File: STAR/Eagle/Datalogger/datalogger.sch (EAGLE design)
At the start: 7 parts, among them J1 J30J-25

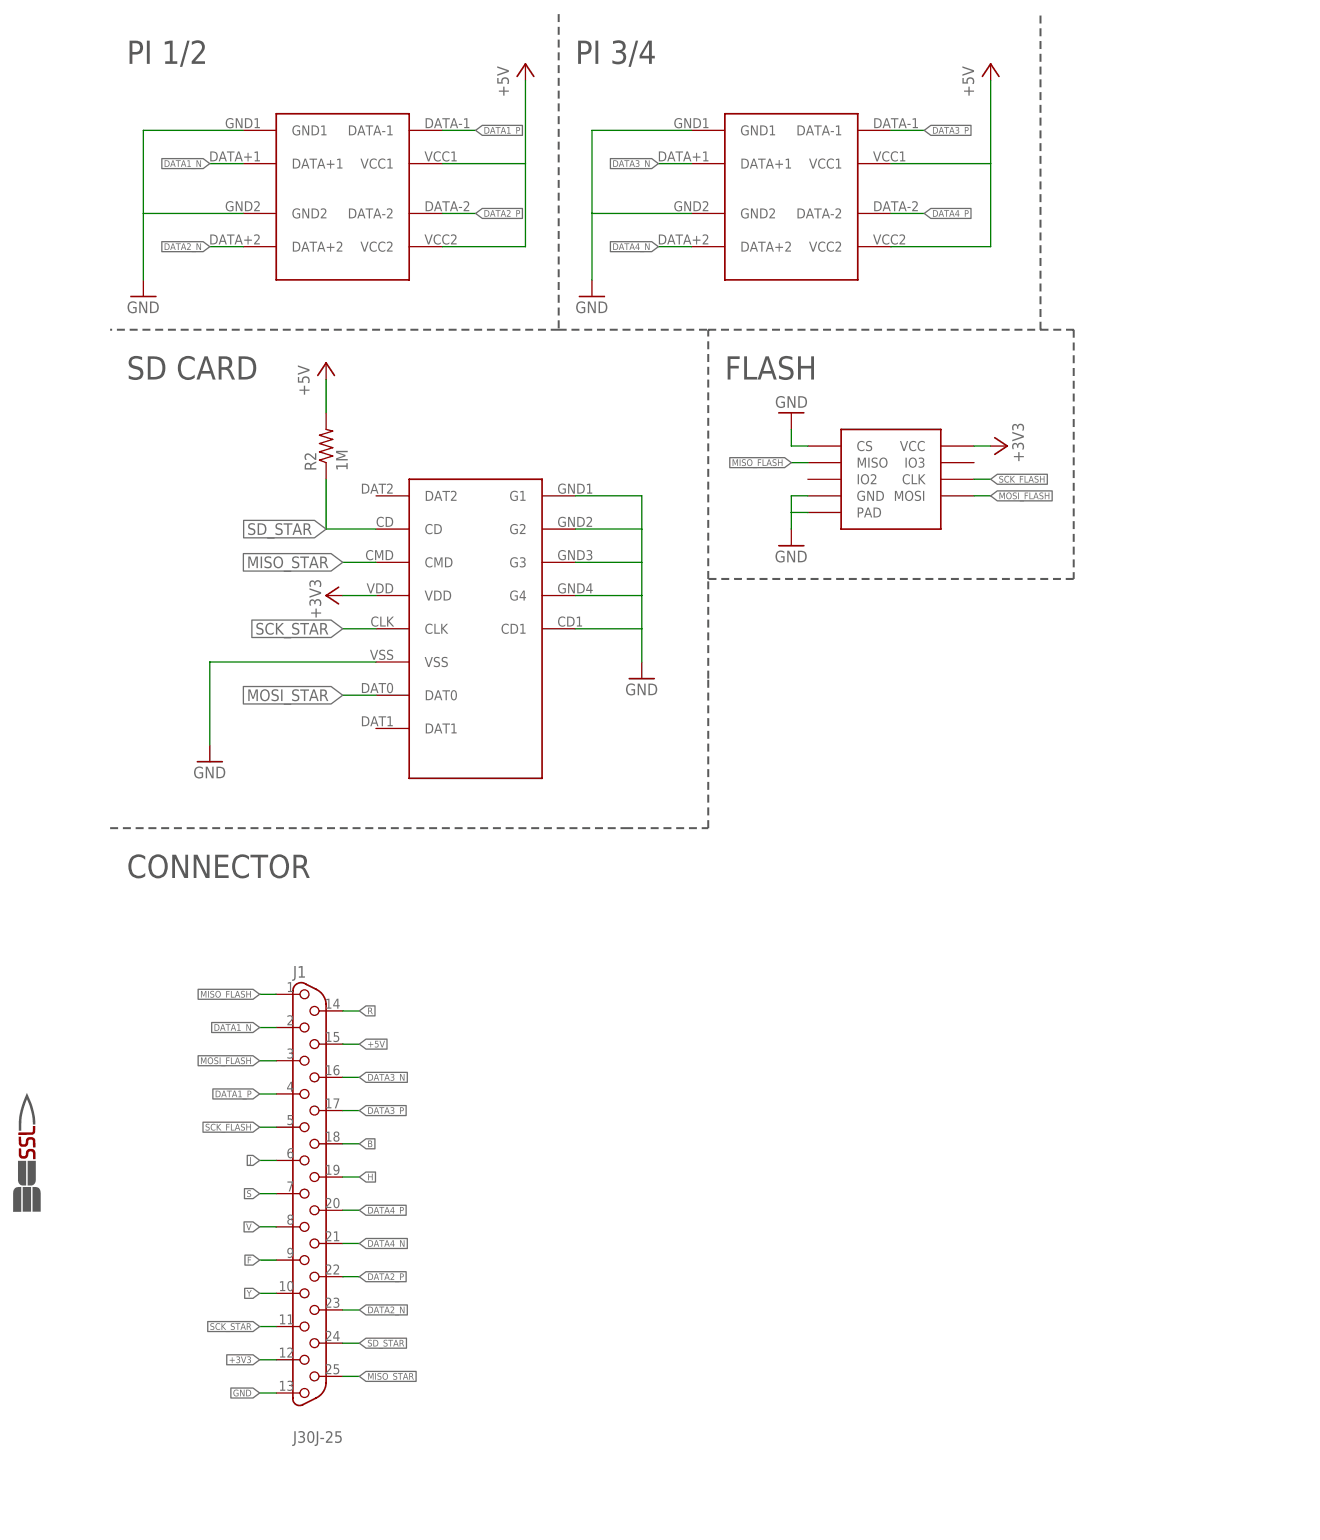
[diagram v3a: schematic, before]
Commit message: datalogger differential pairs
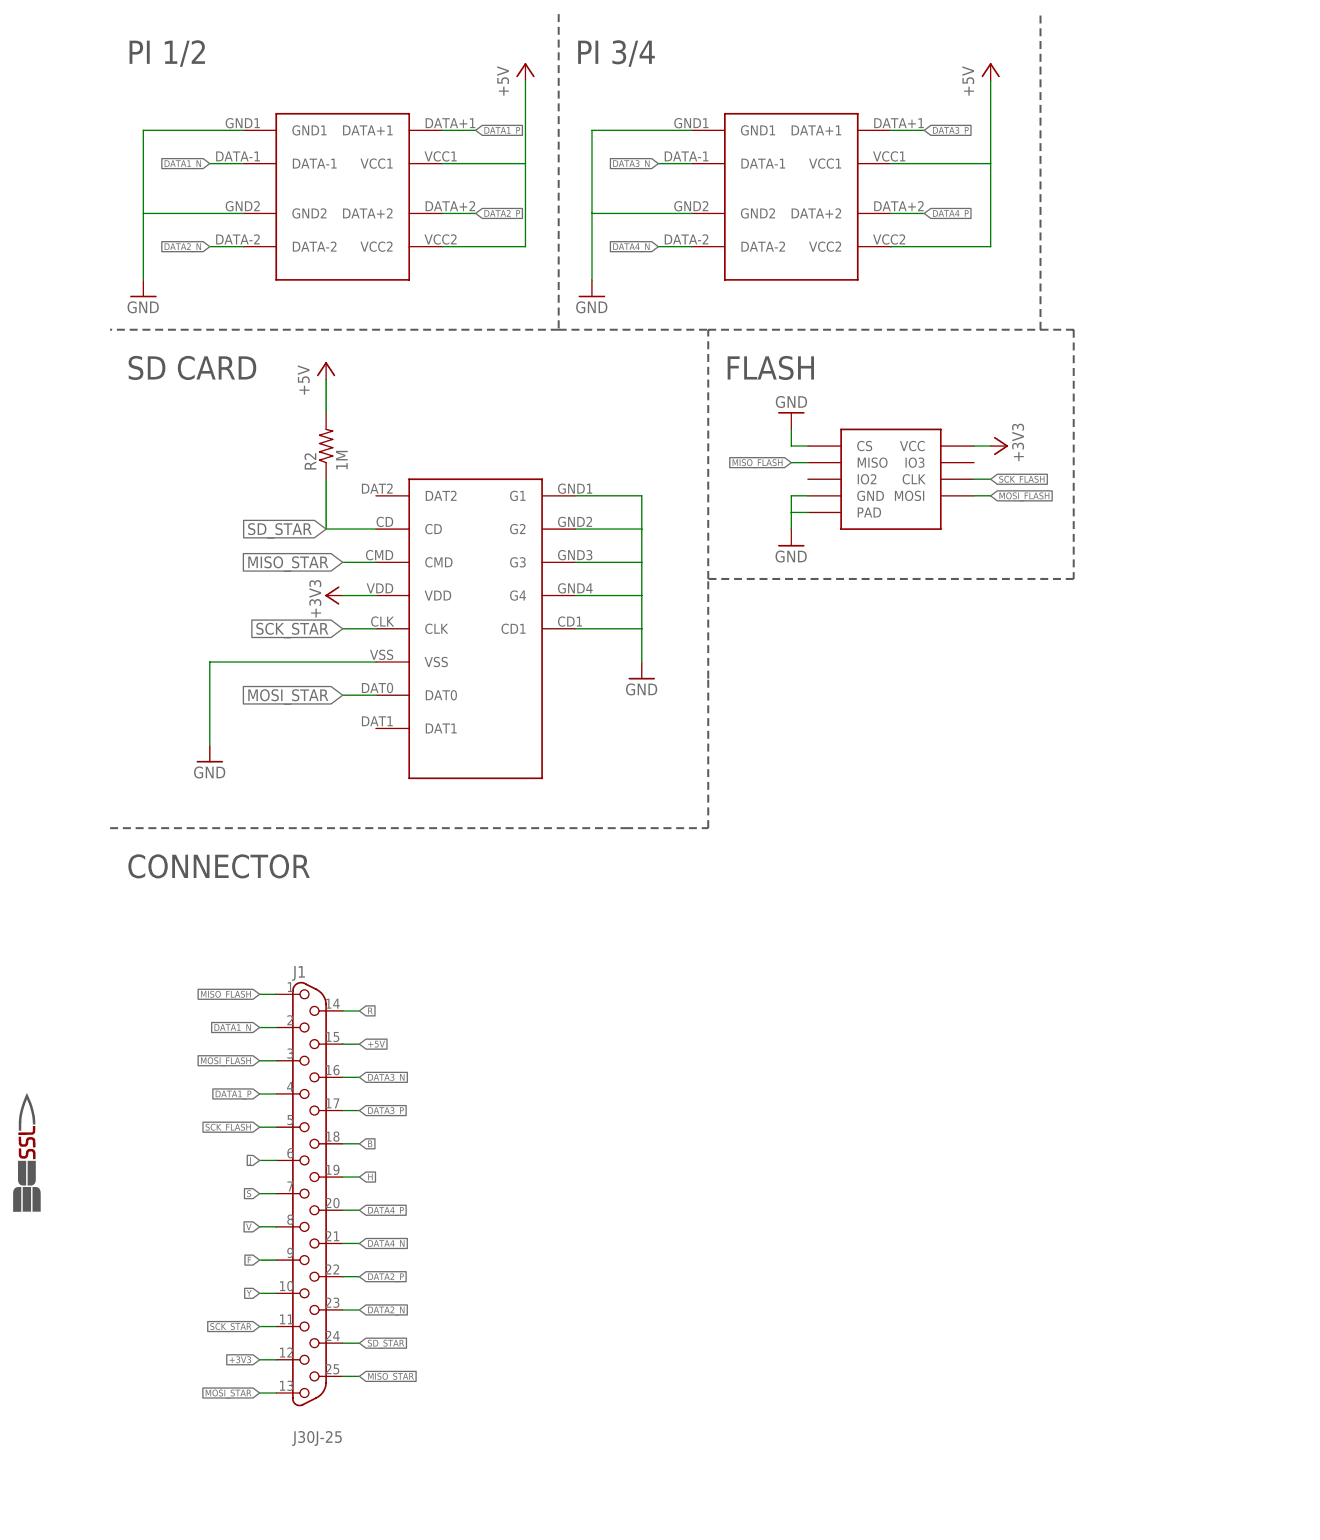
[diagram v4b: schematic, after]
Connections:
- net DATA1_N: now also U$2.DATA-1; no longer U$2.DATA+1
- net DATA1_P: now also U$2.DATA+1; no longer U$2.DATA-1
- net DATA2_N: now also U$2.DATA-2; no longer U$2.DATA+2
- net DATA2_P: now also U$2.DATA+2; no longer U$2.DATA-2
- net DATA3_N: now also U$3.DATA-1; no longer U$3.DATA+1
- net DATA3_P: now also U$3.DATA+1; no longer U$3.DATA-1
- net DATA4_N: now also U$3.DATA-2; no longer U$3.DATA+2
- net DATA4_P: now also U$3.DATA+2; no longer U$3.DATA-2
- net GND: no longer J1.13
- net MOSI_STAR: now also J1.13
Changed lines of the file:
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@@
 <pinref part="GND6" gate="1" pin="GND"/>
-</segment>
-<segment>
-<pinref part="J1" gate="G$1" pin="13"/>
-<wire x1="35.56" y1="60.96" x2="33.02" y2="60.96" width="0.1524" layer="91"/>
-<label x="33.02" y="60.96" size="1.016" layer="95" rot="R180" xref="yes"/>
 </segment>
 </net>
@@
 <label x="45.72" y="167.64" size="1.778" layer="95" rot="R180" xref="yes"/>
 </segment>
+<segment>
+<pinref part="J1" gate="G$1" pin="13"/>
+<wire x1="35.56" y1="60.96" x2="33.02" y2="60.96" width="0.1524" layer="91"/>
+<label x="33.02" y="60.96" size="1.016" layer="95" rot="R180" xref="yes"/>
+</segment>
 </net>
 <net name="SCK_STAR" class="0">
@@
 </segment>
 <segment>
-<pinref part="U$2" gate="G$1" pin="DATA-1"/>
+<pinref part="U$2" gate="G$1" pin="DATA+1"/>
 <wire x1="60.96" y1="254" x2="66.04" y2="254" width="0.1524" layer="91"/>
 <label x="66.04" y="254" size="1.016" layer="95" xref="yes"/>
@@
 </segment>
 <segment>
-<pinref part="U$2" gate="G$1" pin="DATA+1"/>
+<pinref part="U$2" gate="G$1" pin="DATA-1"/>
 <wire x1="30.48" y1="248.92" x2="25.4" y2="248.92" width="0.1524" layer="91"/>
 <label x="25.4" y="248.92" size="1.016" layer="95" rot="R180" xref="yes"/>
@@
 </segment>
 <segment>
-<pinref part="U$2" gate="G$1" pin="DATA-2"/>
+<pinref part="U$2" gate="G$1" pin="DATA+2"/>
 <wire x1="60.96" y1="241.3" x2="66.04" y2="241.3" width="0.1524" layer="91"/>
 <label x="66.04" y="241.3" size="1.016" layer="95" xref="yes"/>
@@
 </segment>
 <segment>
-<pinref part="U$2" gate="G$1" pin="DATA+2"/>
+<pinref part="U$2" gate="G$1" pin="DATA-2"/>
 <wire x1="30.48" y1="236.22" x2="25.4" y2="236.22" width="0.1524" layer="91"/>
 <label x="25.4" y="236.22" size="1.016" layer="95" rot="R180" xref="yes"/>
@@
 </segment>
 <segment>
-<pinref part="U$3" gate="G$1" pin="DATA-1"/>
+<pinref part="U$3" gate="G$1" pin="DATA+1"/>
 <wire x1="129.54" y1="254" x2="134.62" y2="254" width="0.1524" layer="91"/>
 <label x="134.62" y="254" size="1.016" layer="95" xref="yes"/>
@@
 </segment>
 <segment>
-<pinref part="U$3" gate="G$1" pin="DATA+1"/>
+<pinref part="U$3" gate="G$1" pin="DATA-1"/>
 <wire x1="99.06" y1="248.92" x2="93.98" y2="248.92" width="0.1524" layer="91"/>
 <label x="93.98" y="248.92" size="1.016" layer="95" rot="R180" xref="yes"/>
@@
 </segment>
 <segment>
-<pinref part="U$3" gate="G$1" pin="DATA-2"/>
+<pinref part="U$3" gate="G$1" pin="DATA+2"/>
 <wire x1="129.54" y1="241.3" x2="134.62" y2="241.3" width="0.1524" layer="91"/>
 <label x="134.62" y="241.3" size="1.016" layer="95" xref="yes"/>
@@
 </segment>
 <segment>
-<pinref part="U$3" gate="G$1" pin="DATA+2"/>
+<pinref part="U$3" gate="G$1" pin="DATA-2"/>
 <wire x1="99.06" y1="236.22" x2="93.98" y2="236.22" width="0.1524" layer="91"/>
 <label x="93.98" y="236.22" size="1.016" layer="95" rot="R180" xref="yes"/>

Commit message: screws
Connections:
- removed net F: J1.9
- removed net J: J1.6
- removed net R: J1.14
- removed net S: J1.7
- removed net V: J1.8
- removed net Y: J1.10
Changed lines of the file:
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@@
-</segment>
-</net>
-<net name="F" class="0">
-<segment>
-<pinref part="J1" gate="G$1" pin="9"/>
-<wire x1="35.56" y1="81.28" x2="33.02" y2="81.28" width="0.1524" layer="91"/>
-<label x="33.02" y="81.28" size="1.016" layer="95" rot="R180" xref="yes"/>
-</segment>
-</net>
-<net name="Y" class="0">
-<segment>
-<pinref part="J1" gate="G$1" pin="10"/>
-<wire x1="35.56" y1="76.2" x2="33.02" y2="76.2" width="0.1524" layer="91"/>
-<label x="33.02" y="76.2" size="1.016" layer="95" rot="R180" xref="yes"/>
-</segment>
-</net>
-<net name="S" class="0">
-<segment>
-<pinref part="J1" gate="G$1" pin="7"/>
-<wire x1="35.56" y1="91.44" x2="33.02" y2="91.44" width="0.1524" layer="91"/>
-<label x="33.02" y="91.44" size="1.016" layer="95" rot="R180" xref="yes"/>
 </segment>
 </net>
@@
 <pinref part="J1" gate="G$1" pin="18"/>
 <wire x1="45.72" y1="99.06" x2="48.26" y2="99.06" width="0.1524" layer="91"/>
-<label x="48.26" y="99.06" size="1.016" layer="95" xref="yes"/>
-</segment>
-</net>
-<net name="V" class="0">
-<segment>
-<pinref part="J1" gate="G$1" pin="8"/>
-<wire x1="35.56" y1="86.36" x2="33.02" y2="86.36" width="0.1524" layer="91"/>
-<label x="33.02" y="86.36" size="1.016" layer="95" rot="R180" xref="yes"/>
-</segment>
-</net>
-<net name="J" class="0">
-<segment>
-<pinref part="J1" gate="G$1" pin="6"/>
-<wire x1="35.56" y1="96.52" x2="33.02" y2="96.52" width="0.1524" layer="91"/>
-<label x="33.02" y="96.52" size="1.016" layer="95" rot="R180" xref="yes"/>
 </segment>
 </net>
@@
 <pinref part="J1" gate="G$1" pin="19"/>
 <wire x1="45.72" y1="93.98" x2="48.26" y2="93.98" width="0.1524" layer="91"/>
-<label x="48.26" y="93.98" size="1.016" layer="95" xref="yes"/>
 </segment>
 </net>
-<net name="R" class="0">
-<segment>
-<pinref part="J1" gate="G$1" pin="14"/>
-<wire x1="45.72" y1="119.38" x2="48.26" y2="119.38" width="0.1524" layer="91"/>
-<label x="48.26" y="119.38" size="1.016" layer="95" xref="yes"/>
-</segment>
-</net>

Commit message: datalogger 2.1
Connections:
- removed net B: J1.18
- removed net H: J1.19
- net GND: now also J1.18
- net MISO_STAR: now also J1.13, U$1.DAT0; no longer J1.25, U$1.CMD
- net MOSI_STAR: now also J1.25, U$1.CMD; no longer J1.13, U$1.DAT0
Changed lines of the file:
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@@
 <pinref part="GND6" gate="1" pin="GND"/>
+</segment>
+<segment>
+<pinref part="J1" gate="G$1" pin="18"/>
+<wire x1="45.72" y1="99.06" x2="48.26" y2="99.06" width="0.1524" layer="91"/>
+<label x="48.26" y="99.06" size="1.016" layer="95" xref="yes"/>
 </segment>
 </net>
@@
 </segment>
 </net>
-<net name="MISO_STAR" class="0">
+<net name="MOSI_STAR" class="0">
 <segment>
 <pinref part="U$1" gate="G$1" pin="CMD"/>
@@
 </segment>
 </net>
-<net name="MOSI_STAR" class="0">
+<net name="MISO_STAR" class="0">
 <segment>
 <pinref part="U$1" gate="G$1" pin="DAT0"/>
@@
 </segment>
 </net>
-<net name="B" class="0">
-<segment>
-<pinref part="J1" gate="G$1" pin="18"/>
-<wire x1="45.72" y1="99.06" x2="48.26" y2="99.06" width="0.1524" layer="91"/>
-</segment>
-</net>
-<net name="H" class="0">
-<segment>
-<pinref part="J1" gate="G$1" pin="19"/>
-<wire x1="45.72" y1="93.98" x2="48.26" y2="93.98" width="0.1524" layer="91"/>
-</segment>
-</net>

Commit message: CAM and Datalogger 2.2
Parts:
- removed U$5: W25N01GV, NR_IC:W25N01GV
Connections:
- removed net MISO_FLASH: J1.1, U$5.MISO
- removed net MOSI_FLASH: J1.3, U$5.MOSI
- removed net SCK_FLASH: J1.5, U$5.CLK
- new net N$1: J1.14
- new net N$2: J1.15
- new net N$4: J1.6
- new net N$5: J1.7
- new net N$6: J1.8
- new net N$7: J1.9
- new net N$8: J1.10
- net +3V3: no longer U$5.VCC
- net +5V: now also J1.1, J1.19; no longer J1.15
- net GND: no longer U$5.CS, U$5.GND, U$5.PAD
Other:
- note removed: "FLASH"
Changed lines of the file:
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@@
 <part name="+3V2" library="supply1" deviceset="+3V3" device=""/>
 <part name="U$4" library="images" deviceset="SSL" device=".3IN_SILK"/>
-<part name="U$5" library="NR_IC" deviceset="W25N01GV" device=""/>
-<part name="GND3" library="supply1" deviceset="GND" device=""/>
-<part name="GND6" library="supply1" deviceset="GND" device=""/>
 <part name="J1" library="CM_J30J" deviceset="J30J-25" device=""/>
-<part name="+3V1" library="supply1" deviceset="+3V3" device=""/>
 </parts>
 <sheets>
@@
 <wire x1="101.6" y1="170.18" x2="101.6" y2="185.42" width="0.3048" layer="97" style="shortdash"/>
 <wire x1="101.6" y1="185.42" x2="101.6" y2="223.52" width="0.3048" layer="97" style="shortdash"/>
-<text x="104.14" y="215.9" size="3.556" layer="97">FLASH</text>
-<wire x1="152.4" y1="223.52" x2="157.48" y2="223.52" width="0.3048" layer="97" style="shortdash"/>
-<wire x1="157.48" y1="223.52" x2="157.48" y2="185.42" width="0.3048" layer="97" style="shortdash"/>
-<wire x1="157.48" y1="185.42" x2="101.6" y2="185.42" width="0.3048" layer="97" style="shortdash"/>
 </plain>
 <instances>
@@
 </instance>
 <instance part="U$4" gate="G$1" x="-2.54" y="96.52"/>
-<instance part="U$5" gate="G$1" x="129.54" y="200.66"/>
-<instance part="GND3" gate="1" x="114.3" y="190.5"/>
-<instance part="GND6" gate="1" x="114.3" y="210.82" rot="R180"/>
 <instance part="J1" gate="G$1" x="40.64" y="91.44"/>
-<instance part="+3V1" gate="G$1" x="147.32" y="205.74" smashed="yes" rot="R270">
-<attribute name="VALUE" x="149.86" y="203.2" size="1.778" layer="96" rot="R90"/>
-</instance>
 </instances>
 <busses>
@@
 </segment>
 <segment>
-<pinref part="U$5" gate="G$1" pin="GND"/>
-<wire x1="116.84" y1="198.12" x2="114.3" y2="198.12" width="0.1524" layer="91"/>
-<wire x1="114.3" y1="198.12" x2="114.3" y2="195.58" width="0.1524" layer="91"/>
-<pinref part="U$5" gate="G$1" pin="PAD"/>
-<wire x1="114.3" y1="195.58" x2="114.3" y2="193.04" width="0.1524" layer="91"/>
-<wire x1="116.84" y1="195.58" x2="114.3" y2="195.58" width="0.1524" layer="91"/>
-<pinref part="GND3" gate="1" pin="GND"/>
-</segment>
-<segment>
-<pinref part="U$5" gate="G$1" pin="CS"/>
-<wire x1="116.84" y1="205.74" x2="114.3" y2="205.74" width="0.1524" layer="91"/>
-<wire x1="114.3" y1="205.74" x2="114.3" y2="208.28" width="0.1524" layer="91"/>
-<pinref part="GND6" gate="1" pin="GND"/>
-</segment>
-<segment>
 <pinref part="J1" gate="G$1" pin="18"/>
 <wire x1="45.72" y1="99.06" x2="48.26" y2="99.06" width="0.1524" layer="91"/>
@@
 <wire x1="50.8" y1="182.88" x2="45.72" y2="182.88" width="0.1524" layer="91"/>
 <pinref part="+3V2" gate="G$1" pin="+3V3"/>
-</segment>
-<segment>
-<pinref part="U$5" gate="G$1" pin="VCC"/>
-<wire x1="142.24" y1="205.74" x2="144.78" y2="205.74" width="0.1524" layer="91"/>
-<pinref part="+3V1" gate="G$1" pin="+3V3"/>
 </segment>
 <segment>
@@
 </segment>
 <segment>
-<pinref part="J1" gate="G$1" pin="15"/>
-<wire x1="45.72" y1="114.3" x2="48.26" y2="114.3" width="0.1524" layer="91"/>
-<label x="48.26" y="114.3" size="1.016" layer="95" xref="yes"/>
+<pinref part="J1" gate="G$1" pin="19"/>
+<wire x1="45.72" y1="93.98" x2="48.26" y2="93.98" width="0.1524" layer="91"/>
+<label x="48.26" y="93.98" size="1.016" layer="95" xref="yes"/>
+</segment>
+<segment>
+<pinref part="J1" gate="G$1" pin="1"/>
+<wire x1="35.56" y1="121.92" x2="33.02" y2="121.92" width="0.1524" layer="91"/>
+<label x="33.02" y="121.92" size="1.016" layer="95" rot="R180" xref="yes"/>
 </segment>
 </net>
@@
 </segment>
 </net>
-<net name="SCK_FLASH" class="0">
-<segment>
-<pinref part="U$5" gate="G$1" pin="CLK"/>
-<wire x1="142.24" y1="200.66" x2="144.78" y2="200.66" width="0.1524" layer="91"/>
-<label x="144.78" y="200.66" size="1.016" layer="95" xref="yes"/>
-</segment>
-<segment>
-<pinref part="J1" gate="G$1" pin="5"/>
-<wire x1="35.56" y1="101.6" x2="33.02" y2="101.6" width="0.1524" layer="91"/>
-<label x="33.02" y="101.6" size="1.016" layer="95" rot="R180" xref="yes"/>
-</segment>
-</net>
-<net name="MOSI_FLASH" class="0">
-<segment>
-<pinref part="U$5" gate="G$1" pin="MOSI"/>
-<wire x1="142.24" y1="198.12" x2="144.78" y2="198.12" width="0.1524" layer="91"/>
-<label x="144.78" y="198.12" size="1.016" layer="95" xref="yes"/>
-</segment>
-<segment>
-<pinref part="J1" gate="G$1" pin="3"/>
-<wire x1="35.56" y1="111.76" x2="33.02" y2="111.76" width="0.1524" layer="91"/>
-<label x="33.02" y="111.76" size="1.016" layer="95" rot="R180" xref="yes"/>
-</segment>
-</net>
-<net name="MISO_FLASH" class="0">
-<segment>
-<pinref part="U$5" gate="G$1" pin="MISO"/>
-<wire x1="116.84" y1="203.2" x2="114.3" y2="203.2" width="0.1524" layer="91"/>
-<label x="114.3" y="203.2" size="1.016" layer="95" rot="R180" xref="yes"/>
-</segment>
-<segment>
-<pinref part="J1" gate="G$1" pin="1"/>
-<wire x1="35.56" y1="121.92" x2="33.02" y2="121.92" width="0.1524" layer="91"/>
-<label x="33.02" y="121.92" size="1.016" layer="95" rot="R180" xref="yes"/>
-</segment>
-</net>
+<net name="N$1" class="0">
+<segment>
+<pinref part="J1" gate="G$1" pin="14"/>
+<wire x1="45.72" y1="119.38" x2="48.26" y2="119.38" width="0.1524" layer="91"/>
+</segment>
+</net>
+<net name="N$2" class="0">
+<segment>
+<pinref part="J1" gate="G$1" pin="15"/>
+<wire x1="45.72" y1="114.3" x2="48.26" y2="114.3" width="0.1524" layer="91"/>
+</segment>
+</net>
+<net name="N$4" class="0">
+<segment>
+<pinref part="J1" gate="G$1" pin="6"/>
+<wire x1="35.56" y1="96.52" x2="33.02" y2="96.52" width="0.1524" layer="91"/>
+</segment>
+</net>
+<net name="N$5" class="0">
+<segment>
+<pinref part="J1" gate="G$1" pin="7"/>
+<wire x1="35.56" y1="91.44" x2="33.02" y2="91.44" width="0.1524" layer="91"/>
+</segment>
+</net>
+<net name="N$6" class="0">
+<segment>
+<pinref part="J1" gate="G$1" pin="8"/>
+<wire x1="35.56" y1="86.36" x2="33.02" y2="86.36" width="0.1524" layer="91"/>
+</segment>
+</net>
+<net name="N$7" class="0">
+<segment>
+<pinref part="J1" gate="G$1" pin="9"/>
+<wire x1="35.56" y1="81.28" x2="33.02" y2="81.28" width="0.1524" layer="91"/>
+</segment>
+</net>
+<net name="N$8" class="0">
+<segment>
+<pinref part="J1" gate="G$1" pin="10"/>
+<wire x1="35.56" y1="76.2" x2="33.02" y2="76.2" width="0.1524" layer="91"/>
+</segment>
+</net>
